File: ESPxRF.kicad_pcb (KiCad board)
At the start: 4 copper layers, 67.6 x 28.7 mm, 37 parts, among them J1 USB_C_Receptacle_USB2.0, J2 ANT, U1 NCP115ASN330T2G, U2 NRF24L01, U3 USBLC6-2SC6, U4 ESP32-S3, Y1 Crystal_GND24_Small

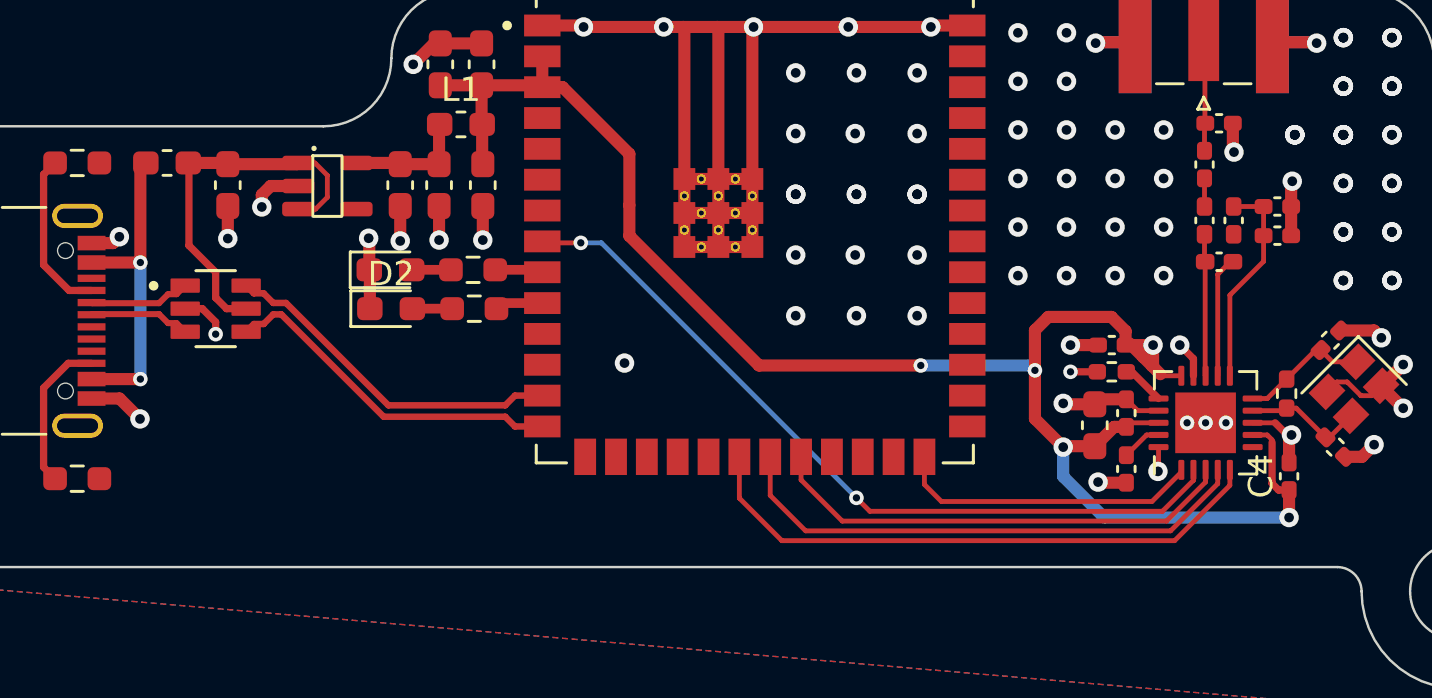
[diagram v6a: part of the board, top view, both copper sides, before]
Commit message: added silkscreen name
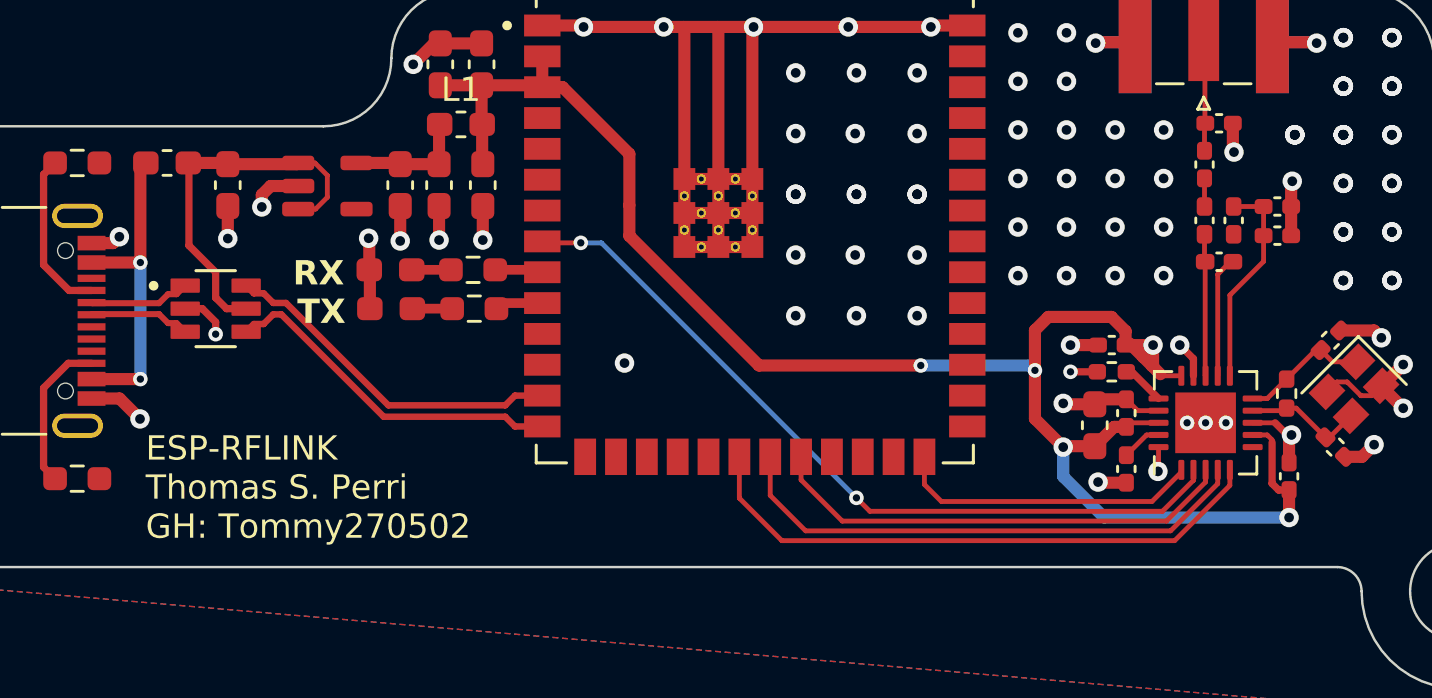
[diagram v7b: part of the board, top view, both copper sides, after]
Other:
- board text added: "ESP-RFLINK Thomas S. Perri GH: Tommy270502"
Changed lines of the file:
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@@
     (pad "4" smd rect (at -0.875 -0.7 225) (size 1.15 1) (layers "F.Cu" "F.Paste" "F.Mask")
       (net 22 "GND") (pinfunction "4") (pintype "passive"))
-    (model "C:/Program Files/KiCad/6.0/share/kicad/3dmodels/Crystal.3dshapes/ECS-160-9-36B-CKY-TR.STEP"
+    (model "${KIPRJMOD}/KicadLibs/Crystal/ECS-160-9-36B-CKY-TR.STEP"
       (offset (xyz 0 0 0))
       (scale (xyz 1 1 1))
@@
     (property "ki_keywords" "capacitor cap")
     (attr smd)
-    (fp_text reference "C4" (at 0 -1.16 90) (layer "F.SilkS")
+    (fp_text reference "C4" (at 0 -1.16 90) (layer "F.SilkS") hide
         (effects (font (size 1 1) (thickness 0.15)))
     )
@@
         (effects (font (size 1 1) (thickness 0.15)))
     )
-    (fp_rect (start -0.6 -1.25) (end 0.6 1.25)
-      (stroke (width 0.12) (type solid)) (fill none) (layer "F.SilkS"))
-    (fp_circle (center -0.55 -1.55) (end -0.5 -1.55)
-      (stroke (width 0.12) (type solid)) (fill none) (layer "F.SilkS"))
     (pad "1" smd roundrect (at -1.2 -0.95) (size 1.325 0.6) (layers "F.Cu" "F.Paste" "F.Mask") (roundrect_rratio 0.25)
       (net 21 "+5V") (pinfunction "in") (pintype "input"))
@@
         (effects (font (size 0.4 0.4) (thickness 0.06)))
     )
-    (fp_line (start -1.66 -0.735) (end -1.66 0.735)
-      (stroke (width 0.12) (type solid)) (layer "F.SilkS"))
-    (fp_line (start -1.66 0.735) (end 0.8 0.735)
-      (stroke (width 0.12) (type solid)) (layer "F.SilkS"))
-    (fp_line (start 0.8 -0.735) (end -1.66 -0.735)
-      (stroke (width 0.12) (type solid)) (layer "F.SilkS"))
     (fp_line (start -1.65 -0.73) (end 1.65 -0.73)
       (stroke (width 0.05) (type solid)) (layer "F.CrtYd"))
@@
     (property "ki_keywords" "LED diode light-emitting-diode")
     (attr smd)
-    (fp_text reference "D2" (at 0 -1.43) (layer "F.SilkS")
+    (fp_text reference "D2" (at 0 -1.43) (layer "F.SilkS") hide
         (effects (font (size 1 1) (thickness 0.15)))
     )
@@
         (effects (font (size 0.4 0.4) (thickness 0.06)))
     )
-    (fp_line (start -1.66 -0.735) (end -1.66 0.735)
-      (stroke (width 0.12) (type solid)) (layer "F.SilkS"))
-    (fp_line (start -1.66 0.735) (end 0.8 0.735)
-      (stroke (width 0.12) (type solid)) (layer "F.SilkS"))
-    (fp_line (start 0.8 -0.735) (end -1.66 -0.735)
-      (stroke (width 0.12) (type solid)) (layer "F.SilkS"))
     (fp_line (start -1.65 -0.73) (end 1.65 -0.73)
       (stroke (width 0.05) (type solid)) (layer "F.CrtYd"))
@@
   (gr_line (start 86.3 67.35) (end 86.3 80.5)
     (stroke (width 0.1) (type default)) (layer "Edge.Cuts"))
-  (gr_text "TX" (at 102.365 73.16) (layer "F.Fab")
+  (gr_text "ESP-RFLINK\nThomas S. Perri\nGH: Tommy270502" (at 95.885 81.915) (layer "F.SilkS")
+    (effects (font (size 1 1) (thickness 0.15)) (justify left bottom))
+  )
+  (gr_text "TX" (at 102.124073 73.066722) (layer "F.SilkS")
     (effects (font (size 1 1) (thickness 0.25) bold) (justify left bottom))
   )
-  (gr_text "RX" (at 102.165 71.56) (layer "F.Fab")
+  (gr_text "RX" (at 101.943967 71.481784) (layer "F.SilkS")
     (effects (font (size 1 1) (thickness 0.25) bold) (justify left bottom))
   )

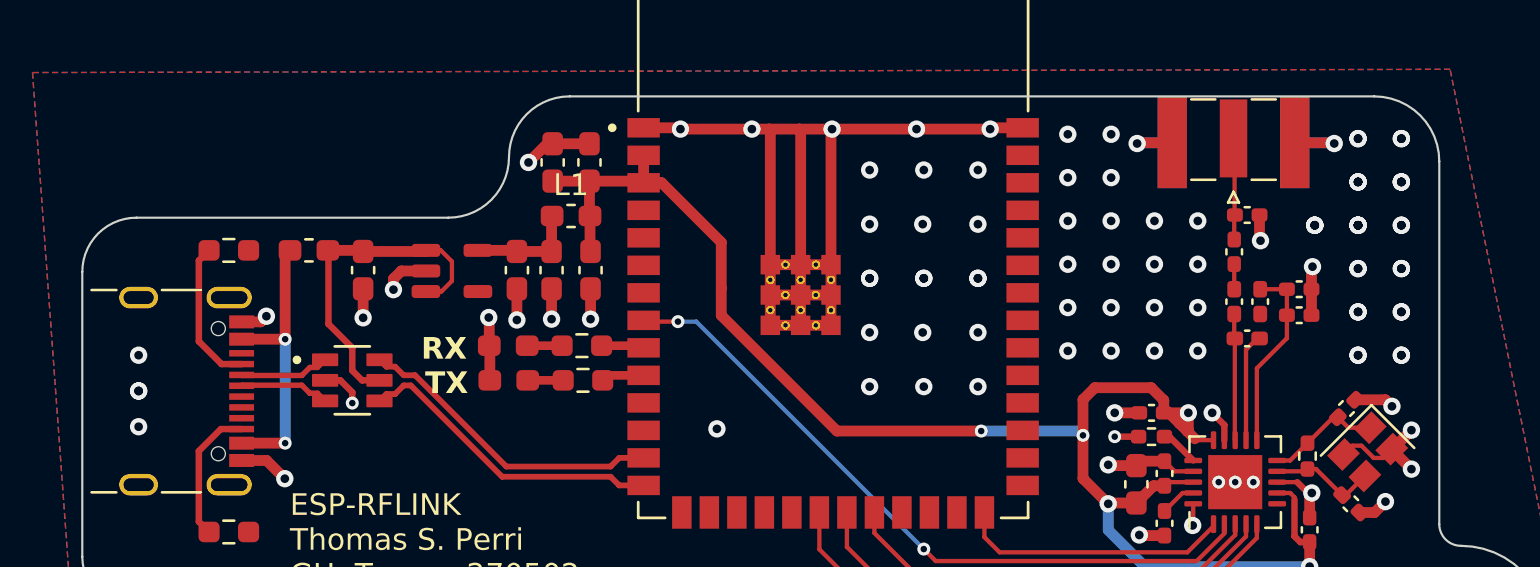
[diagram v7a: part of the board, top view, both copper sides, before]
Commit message: went through the DRC and assigned my own kicad libraries
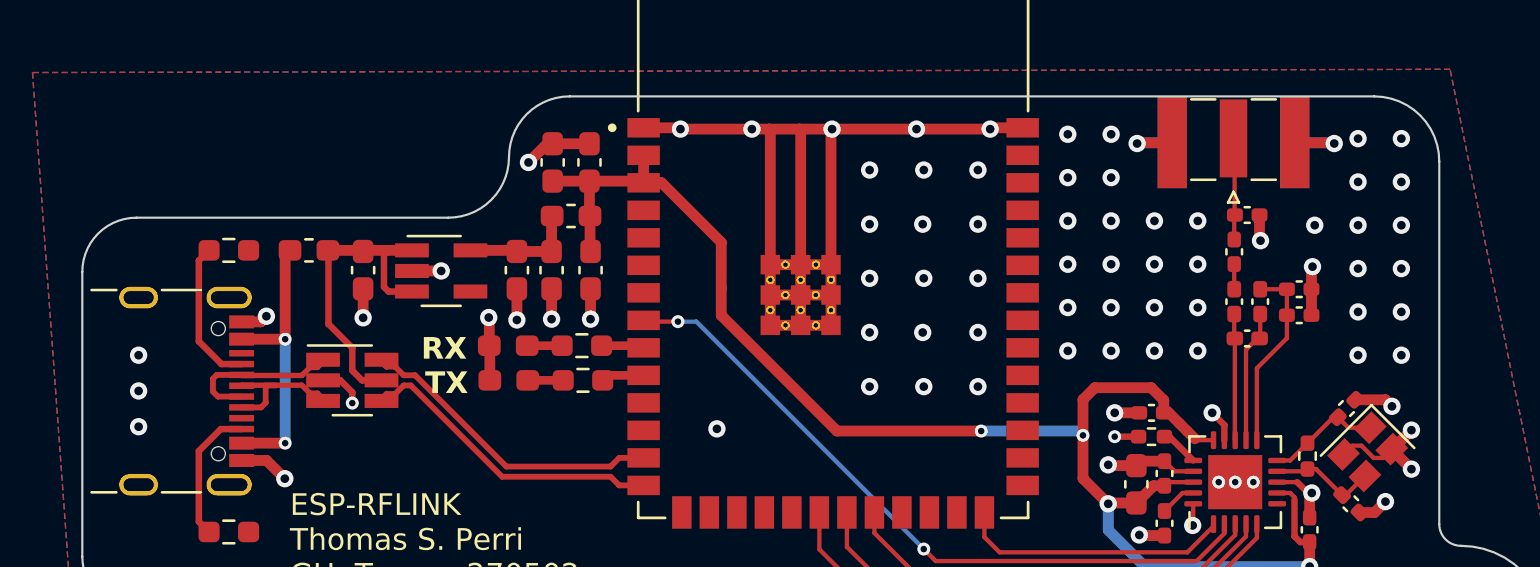
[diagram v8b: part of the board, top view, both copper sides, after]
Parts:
- U1: footprint NCP115ASN330T2G:NCP115ASN330T2G -> Package_TO_SOT_SMD:SOT-23-5_HandSoldering
- U3: footprint SnapEda:SOT95P280X145-6N -> Package_TO_SOT_SMD:SOT-23-6_Handsoldering
- moved U1 0.49 mm to (102.9, 67.3)
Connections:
- U4 pad 41_10: (no net) -> GND
- U4 pad 41_11: (no net) -> GND
- U4 pad 41_12: (no net) -> GND
- U4 pad 41_13: (no net) -> GND
- U4 pad 41_14: (no net) -> GND
- U4 pad 41_15: (no net) -> GND
- U4 pad 41_16: (no net) -> GND
- U4 pad 41_17: (no net) -> GND
- U4 pad 41_18: (no net) -> GND
- U4 pad 41_19: (no net) -> GND
- U4 pad 41_20: (no net) -> GND
- U4 pad 41_21: (no net) -> GND
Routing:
- net USBCON_D-: track 4.17 -> 7.57 mm
- net +3V3: track 71.6 -> 68.9 mm, vias 5 -> 4
- net USBCON_D+: track 4.17 -> 6.65 mm
- net +5V: track 15.7 -> 14.5 mm
- net ANT1: track 5.02 -> 6.16 mm
- net GND: track 106.4 -> 105.6 mm, vias 108 -> 85
